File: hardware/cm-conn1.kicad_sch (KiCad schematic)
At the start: 6 parts, among them J4 RJ45_RB1-125B8G1A

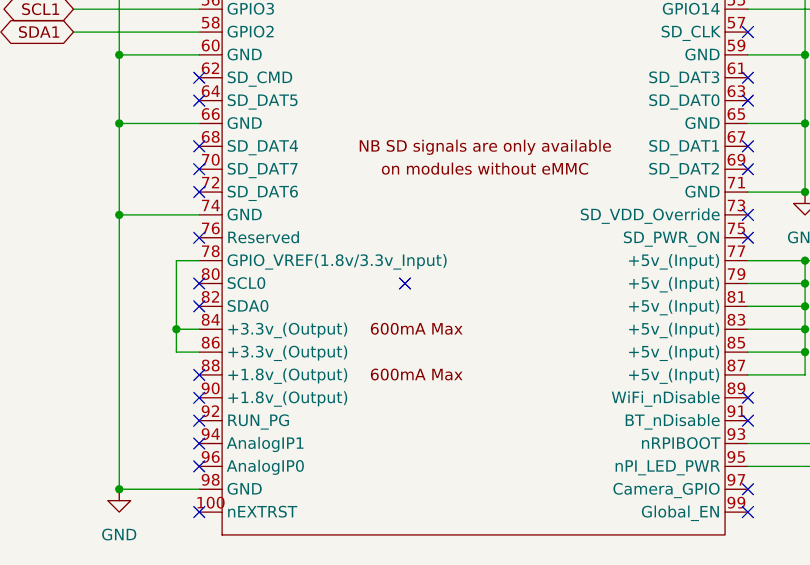
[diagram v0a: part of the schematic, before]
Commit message: ERC: 0 errors, 0 warnings — fully clean
- Fix ASM1061 footprint reference (granit:QFN50P700X700X90-49N-D)
- Fix CM4 embedded symbol references (pedalboard → granit)
- Sync ASM1061 embedded symbol with library
- Remove dangling no-connect flags
- Re-add NC for barrel jack switch pin (J7 pin 3)
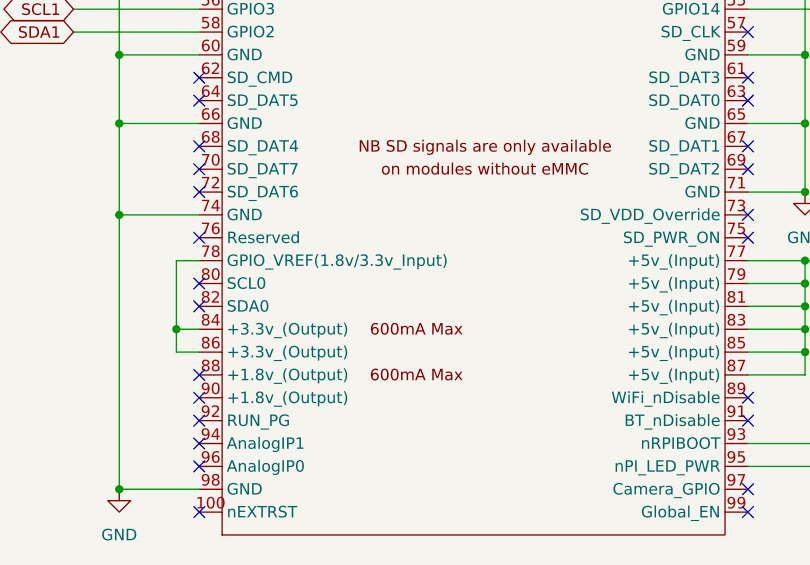
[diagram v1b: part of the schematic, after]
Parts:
- CM1: footprint Pedalboard Library:Raspberry-Pi-4-Compute-Module -> granit:Raspberry-Pi-4-Compute-Module; symbol pedalboard:CM4 -> granit:CM4
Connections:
- no-connect marks 51 -> 50
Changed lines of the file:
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@@
-	)
-	(no_connect
-		(at 77.47 139.7)
 	)
 	(no_connect
@@
 	)
 	(symbol
-		(lib_id "pedalboard:CM4")
+		(lib_id "granit:CM4")
 		(at 87.63 96.52 0)
 		(unit 1)
@@
 			)
 		)
-		(property "Footprint" "Pedalboard Library:Raspberry-Pi-4-Compute-Module"
+		(property "Footprint" "granit:Raspberry-Pi-4-Compute-Module"
 			(at 229.87 123.19 0)
 			(hide yes)

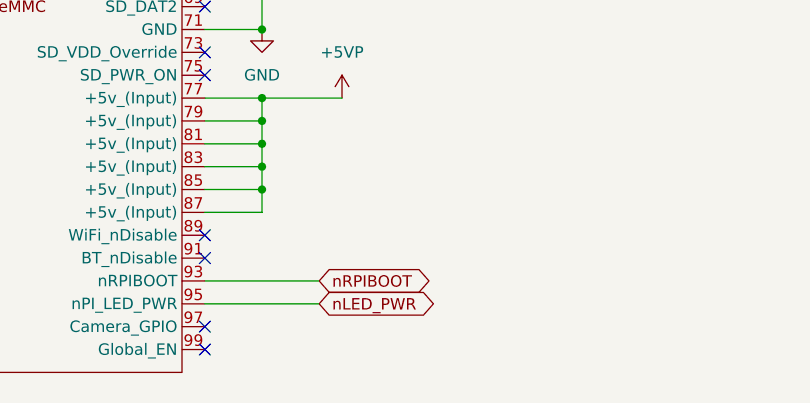
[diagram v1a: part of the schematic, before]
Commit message: Add GLOBAL_EN pull-up for software suspend wake, FIXME for hardware latch
- 10kΩ pull-up on GLOBAL_EN to 3.3V (always-on, software suspend)
- TODO: alternative MOSFET latch for hardware power-off wake
- ERC: 0 errors, 0 warnings
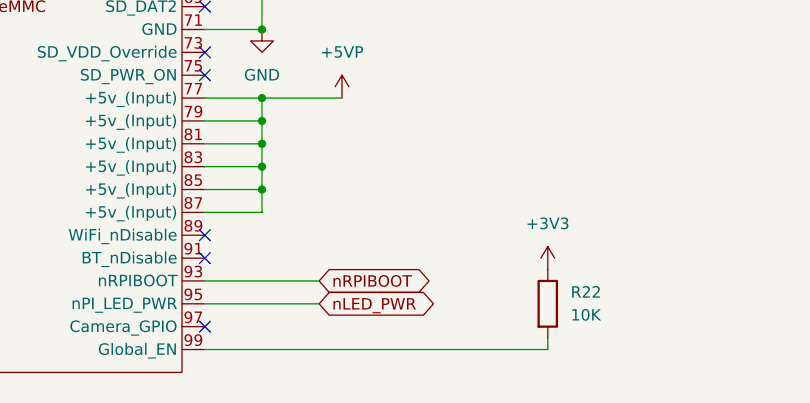
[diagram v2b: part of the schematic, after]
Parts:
- added R22: 10K, symbol Device:R
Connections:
- net +3V3: now also R22.1
- net at CM1.99 (Global_EN): now also R22.2
- no-connect marks 50 -> 49
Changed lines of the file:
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@@
 	)
 	(no_connect
-		(at 115.57 165.1)
-	)
-	(no_connect
 		(at 54.61 60.96)
 	)
@@
 	(wire
 		(pts
+			(xy 115.57 165.1) (xy 153.67 165.1)
+		)
+		(stroke
+			(width 0)
+			(type default)
+		)
+	)
+	(wire
+		(pts
 			(xy 219.71 95.25) (xy 219.71 96.52)
 		)
@@
 	(wire
 		(pts
+			(xy 153.67 163.83) (xy 153.67 165.1)
+		)
+		(stroke
+			(width 0)
+			(type default)
+		)
+	)
+	(wire
+		(pts
 			(xy 121.92 149.86) (xy 121.92 147.32)
 		)
@@
 	)
 	(symbol
+		(lib_id "power:+3V3")
+		(at 153.67 156.21 0)
+		(unit 1)
+		(body_style 1)
+		(exclude_from_sim no)
+		(in_bom yes)
+		(on_board yes)
+		(in_pos_files yes)
+		(dnp no)
+		(fields_autoplaced yes)
+		(property "Reference" "#PWR065"
+			(at 153.67 160.02 0)
+			(hide yes)
+			(show_name no)
+			(do_not_autoplace no)
+			(effects
+				(font
+					(size 1.27 1.27)
+				)
+			)
+		)
+		(property "Value" "+3V3"
+			(at 153.67 151.13 0)
+			(show_name no)
+			(do_not_autoplace no)
+			(effects
+				(font
+					(size 1.27 1.27)
+				)
+			)
+		)
+		(property "Footprint" ""
+			(at 153.67 156.21 0)
+			(hide yes)
+			(show_name no)
+			(do_not_autoplace no)
+			(effects
+				(font
+					(size 1.27 1.27)
+				)
+			)
+		)
+		(property "Datasheet" ""
+			(at 153.67 156.21 0)
+			(hide yes)
+			(show_name no)
+			(do_not_autoplace no)
+			(effects
+				(font
+					(size 1.27 1.27)
+				)
+			)
+		)
+		(property "Description" "Power symbol creates a global label with name \"+3V3\""
+			(at 153.67 156.21 0)
+			(hide yes)
+			(show_name no)
+			(do_not_autoplace no)
+			(effects
+				(font
+					(size 1.27 1.27)
+				)
+			)
+		)
+		(pin "1"
+		)
+		(instances
+			(project "granit"
+				(path "/d2c135e3-a983-4cd4-8cff-b50ca3c7671a/425bdf56-ee3a-43f6-b6d9-8fa9cc85dc16"
+					(reference "#PWR065")
+					(unit 1)
+				)
+			)
+		)
+	)
+	(symbol
 		(lib_id "granit:CM4")
 		(at 87.63 96.52 0)
@@
 					(unit 1)
 				)
+			)
+		)
+	)
+	(symbol
+		(lib_id "Device:R")
+		(at 153.67 160.02 0)
+		(unit 1)
+		(body_style 1)
+		(exclude_from_sim no)
+		(in_bom yes)
+		(on_board yes)
+		(in_pos_files yes)
+		(dnp no)
+		(fields_autoplaced yes)
+		(property "Reference" "R22"
+			(at 156.21 158.7499 0)
+			(show_name no)
+			(do_not_autoplace no)
+			(effects
+				(font
+					(size 1.27 1.27)
+				)
+				(justify left)
+			)
+		)
+		(property "Value" "10K"
+			(at 156.21 161.2899 0)
+			(show_name no)
+			(do_not_autoplace no)
+			(effects
+				(font
+					(size 1.27 1.27)
+				)
+				(justify left)
+			)
+		)
+		(property "Footprint" ""
+			(at 151.892 160.02 90)
+			(hide yes)
+			(show_name no)
+			(do_not_autoplace no)
+			(effects
+				(font
+					(size 1.27 1.27)
+				)
+			)
+		)
+		(property "Datasheet" ""
+			(at 153.67 160.02 0)
+			(hide yes)
+			(show_name no)
+			(do_not_autoplace no)
+			(effects
+				(font
+					(size 1.27 1.27)
+				)
+			)
+		)
+		(property "Description" "Resistor"
+			(at 153.67 160.02 0)
+			(hide yes)
+			(show_name no)
+			(do_not_autoplace no)
+			(effects
+				(font
+					(size 1.27 1.27)
+				)
+			)
+		)
+		(pin "1"
+		)
+		(pin "2"
+		)
+		(instances
+			(project "granit"
+				(path "/d2c135e3-a983-4cd4-8cff-b50ca3c7671a/425bdf56-ee3a-43f6-b6d9-8fa9cc85dc16"
+					(reference "R22")
+					(unit 1)
+				)

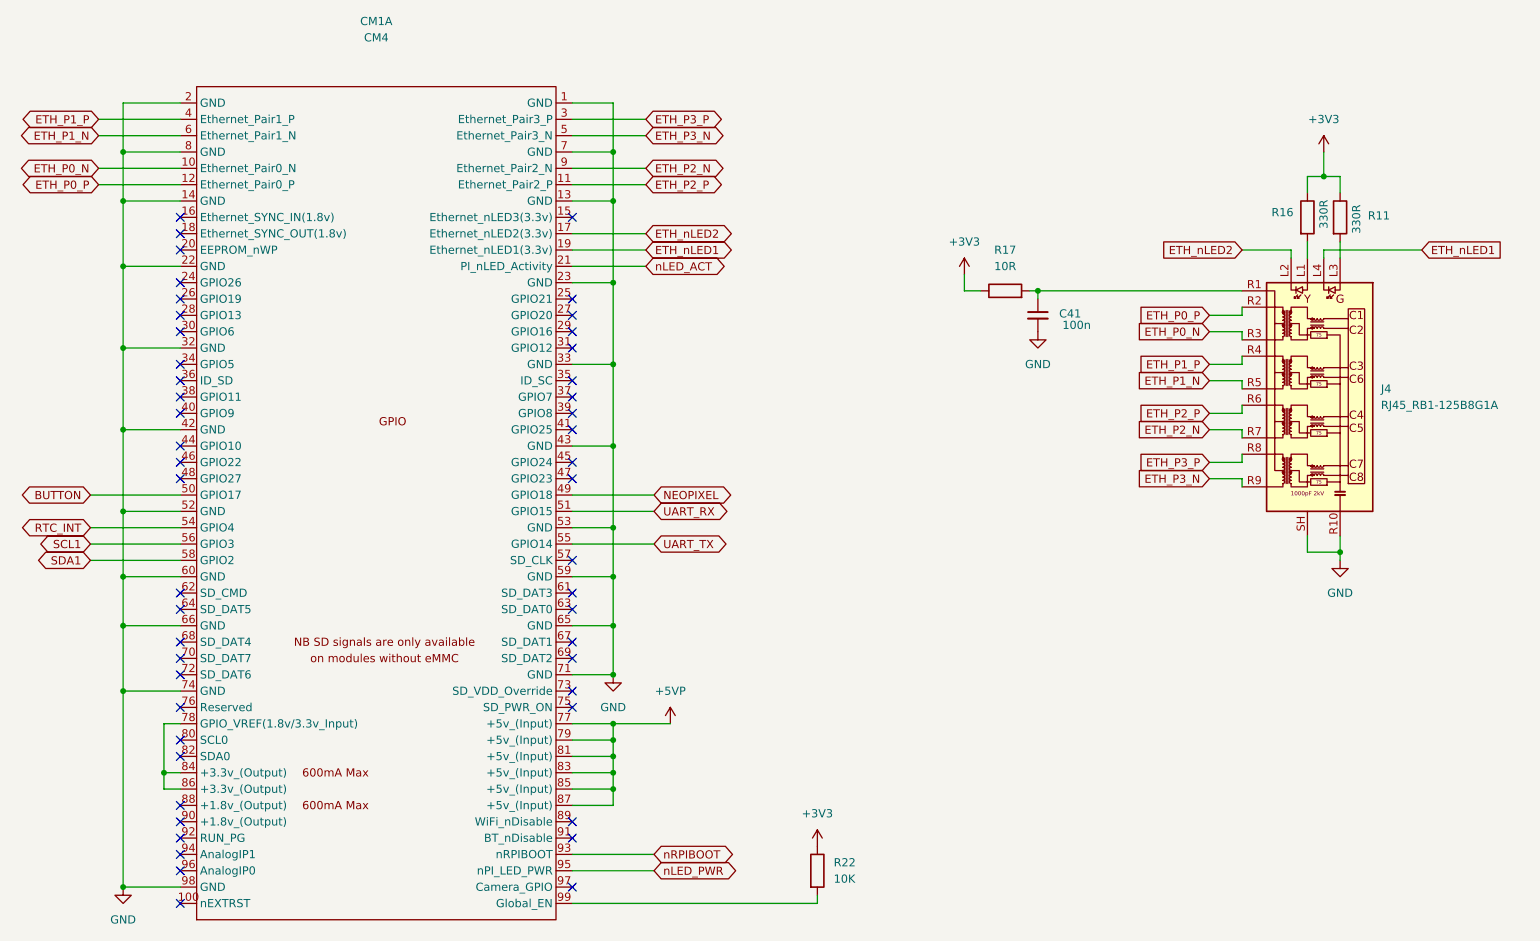
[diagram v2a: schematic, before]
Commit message: Reannotate all components sequentially
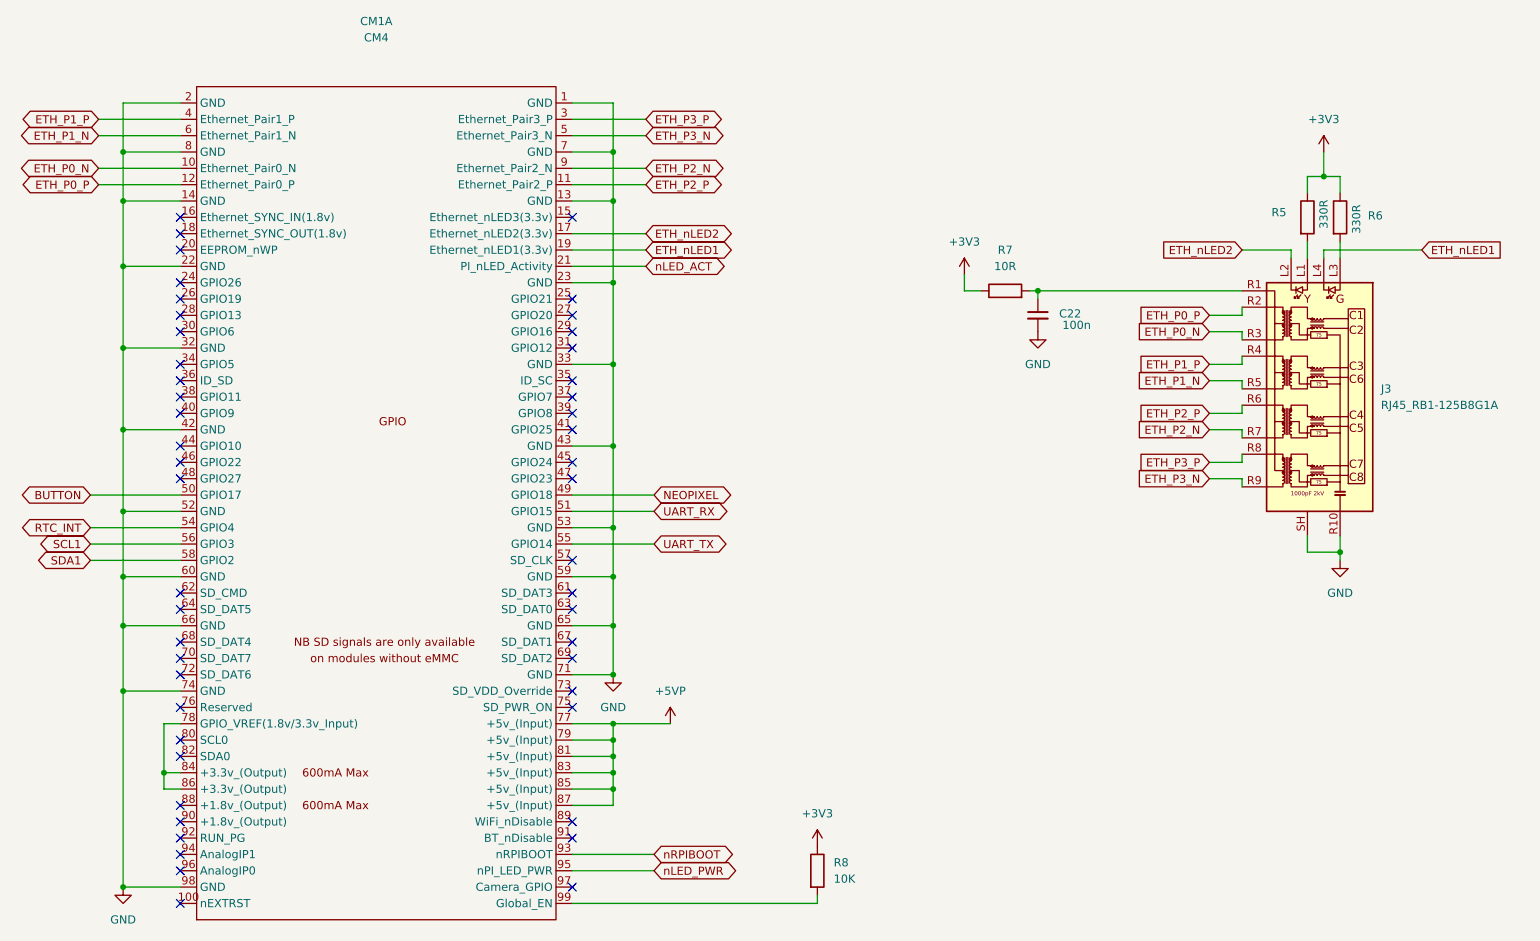
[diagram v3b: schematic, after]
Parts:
- renumbered C41 to C22, J4 to J3, R16 to R5, R11 to R6, R17 to R7, R22 to R8
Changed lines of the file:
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@@
 		(in_pos_files yes)
 		(dnp no)
-		(property "Reference" "C41"
+		(property "Reference" "C22"
 			(at 191.262 73.406 0)
 			(show_name no)
@@
 			(project "granit"
 				(path "/d2c135e3-a983-4cd4-8cff-b50ca3c7671a/425bdf56-ee3a-43f6-b6d9-8fa9cc85dc16"
-					(reference "C41")
+					(reference "C22")
 					(unit 1)
 				)
@@
 		(dnp no)
 		(fields_autoplaced yes)
-		(property "Reference" "#PWR03"
+		(property "Reference" "#PWR020"
 			(at 130.81 140.97 0)
 			(hide yes)
@@
 			(project "granit"
 				(path "/d2c135e3-a983-4cd4-8cff-b50ca3c7671a/425bdf56-ee3a-43f6-b6d9-8fa9cc85dc16"
-					(reference "#PWR03")
+					(reference "#PWR020")
 					(unit 1)
 				)
@@
 		(dnp no)
 		(fields_autoplaced yes)
-		(property "Reference" "#PWR065"
+		(property "Reference" "#PWR021"
 			(at 153.67 160.02 0)
 			(hide yes)
@@
 			(project "granit"
 				(path "/d2c135e3-a983-4cd4-8cff-b50ca3c7671a/425bdf56-ee3a-43f6-b6d9-8fa9cc85dc16"
-					(reference "#PWR065")
+					(reference "#PWR021")
 					(unit 1)
 				)
@@
 		(dnp no)
 		(fields_autoplaced yes)
-		(property "Reference" "#PWR01"
+		(property "Reference" "#PWR019"
 			(at 121.92 135.89 0)
 			(hide yes)
@@
 			(project "granit"
 				(path "/d2c135e3-a983-4cd4-8cff-b50ca3c7671a/425bdf56-ee3a-43f6-b6d9-8fa9cc85dc16"
-					(reference "#PWR01")
+					(reference "#PWR019")
 					(unit 1)
 				)
@@
 		(dnp no)
 		(fields_autoplaced yes)
-		(property "Reference" "#PWR031"
+		(property "Reference" "#PWR018"
 			(at 234.95 118.11 0)
 			(hide yes)
@@
 			(project "granit"
 				(path "/d2c135e3-a983-4cd4-8cff-b50ca3c7671a/425bdf56-ee3a-43f6-b6d9-8fa9cc85dc16"
-					(reference "#PWR031")
+					(reference "#PWR018")
 					(unit 1)
 				)
@@
 		(in_pos_files yes)
 		(dnp no)
-		(property "Reference" "J4"
+		(property "Reference" "J3"
 			(at 241.3 85.0899 0)
 			(show_name no)
@@
 			(project "granit"
 				(path "/d2c135e3-a983-4cd4-8cff-b50ca3c7671a/425bdf56-ee3a-43f6-b6d9-8fa9cc85dc16"
-					(reference "J4")
+					(reference "J3")
 					(unit 1)
 				)
@@
 		(dnp no)
 		(fields_autoplaced yes)
-		(property "Reference" "R17"
+		(property "Reference" "R7"
 			(at 182.88 63.5 90)
 			(show_name no)
@@
 			(project "granit"
 				(path "/d2c135e3-a983-4cd4-8cff-b50ca3c7671a/425bdf56-ee3a-43f6-b6d9-8fa9cc85dc16"
-					(reference "R17")
+					(reference "R7")
 					(unit 1)
 				)
@@
 		(dnp no)
 		(fields_autoplaced yes)
-		(property "Reference" "#PWR027"
+		(property "Reference" "#PWR015"
 			(at 232.41 52.07 0)
 			(hide yes)
@@
 			(project "granit"
 				(path "/d2c135e3-a983-4cd4-8cff-b50ca3c7671a/425bdf56-ee3a-43f6-b6d9-8fa9cc85dc16"
-					(reference "#PWR027")
+					(reference "#PWR015")
 					(unit 1)
 				)
@@
 		(dnp no)
 		(fields_autoplaced yes)
-		(property "Reference" "R22"
+		(property "Reference" "R8"
 			(at 156.21 158.7499 0)
 			(show_name no)
@@
 			(project "granit"
 				(path "/d2c135e3-a983-4cd4-8cff-b50ca3c7671a/425bdf56-ee3a-43f6-b6d9-8fa9cc85dc16"
-					(reference "R22")
+					(reference "R8")
 					(unit 1)
 				)
@@
 		(in_pos_files yes)
 		(dnp no)
-		(property "Reference" "R11"
+		(property "Reference" "R6"
 			(at 239.268 58.166 0)
 			(show_name no)
@@
 			(project "granit"
 				(path "/d2c135e3-a983-4cd4-8cff-b50ca3c7671a/425bdf56-ee3a-43f6-b6d9-8fa9cc85dc16"
-					(reference "R11")
+					(reference "R6")
 					(unit 1)
 				)
@@
 		(dnp no)
 		(fields_autoplaced yes)
-		(property "Reference" "#PWR02"
+		(property "Reference" "#PWR022"
 			(at 45.72 168.91 0)
 			(hide yes)
@@
 			(project "granit"
 				(path "/d2c135e3-a983-4cd4-8cff-b50ca3c7671a/425bdf56-ee3a-43f6-b6d9-8fa9cc85dc16"
-					(reference "#PWR02")
+					(reference "#PWR022")
 					(unit 1)
 				)
@@
 		(dnp no)
 		(fields_autoplaced yes)
-		(property "Reference" "#PWR029"
+		(property "Reference" "#PWR017"
 			(at 187.96 82.55 0)
 			(hide yes)
@@
 			(project "granit"
 				(path "/d2c135e3-a983-4cd4-8cff-b50ca3c7671a/425bdf56-ee3a-43f6-b6d9-8fa9cc85dc16"
-					(reference "#PWR029")
+					(reference "#PWR017")
 					(unit 1)
 				)
@@
 		(in_pos_files yes)
 		(dnp no)
-		(property "Reference" "R16"
+		(property "Reference" "R5"
 			(at 224.282 57.658 0)
 			(show_name no)
@@
 			(project "granit"
 				(path "/d2c135e3-a983-4cd4-8cff-b50ca3c7671a/425bdf56-ee3a-43f6-b6d9-8fa9cc85dc16"
-					(reference "R16")
+					(reference "R5")
 					(unit 1)
 				)
@@
 		(dnp no)
 		(fields_autoplaced yes)
-		(property "Reference" "#PWR028"
+		(property "Reference" "#PWR016"
 			(at 176.53 71.12 0)
 			(hide yes)
@@
 			(project "granit"
 				(path "/d2c135e3-a983-4cd4-8cff-b50ca3c7671a/425bdf56-ee3a-43f6-b6d9-8fa9cc85dc16"
-					(reference "#PWR028")
+					(reference "#PWR016")
 					(unit 1)
 				)

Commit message: Assign footprints to all components
All components now have valid footprints:
- 0805 for all resistors, caps, LEDs
- SOT-23-5/6 for ICs
- 2512 SMD fuse, 3215 crystal
- Pin headers, USB-C, solder jumper, battery holder
- ERC: 0 errors, 0 warnings
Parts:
- R5, R6, R7, R8: footprint (none) -> Resistor_SMD:R_0805_2012Metric
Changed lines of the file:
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@@
 			)
 		)
-		(property "Footprint" ""
+		(property "Footprint" "Resistor_SMD:R_0805_2012Metric"
 			(at 182.88 71.628 90)
 			(hide yes)
@@
 			)
 		)
-		(property "Footprint" ""
+		(property "Footprint" "Resistor_SMD:R_0805_2012Metric"
 			(at 151.892 160.02 90)
 			(hide yes)
@@
 			)
 		)
-		(property "Footprint" ""
+		(property "Footprint" "Resistor_SMD:R_0805_2012Metric"
 			(at 233.172 58.42 90)
 			(hide yes)
@@
 			)
 		)
-		(property "Footprint" ""
+		(property "Footprint" "Resistor_SMD:R_0805_2012Metric"
 			(at 228.092 58.42 90)
 			(hide yes)
